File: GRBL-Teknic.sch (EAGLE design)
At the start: 9 parts

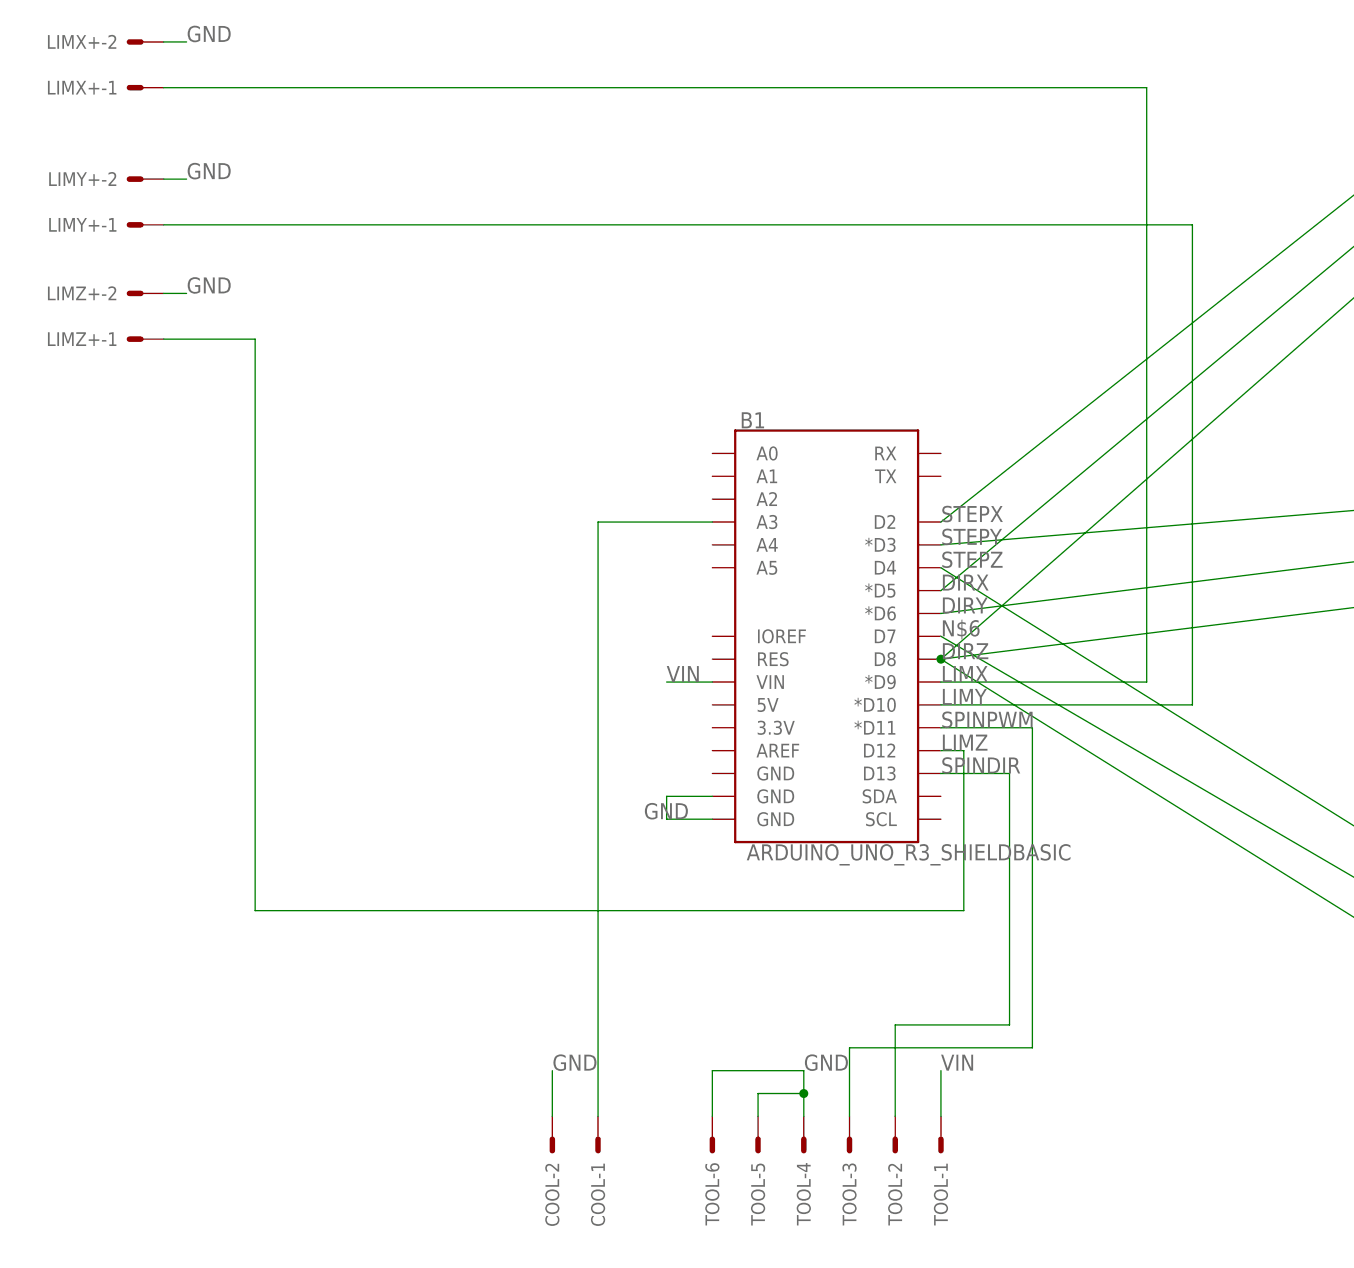
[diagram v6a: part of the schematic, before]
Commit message: updated as I learn more from EMI filtering
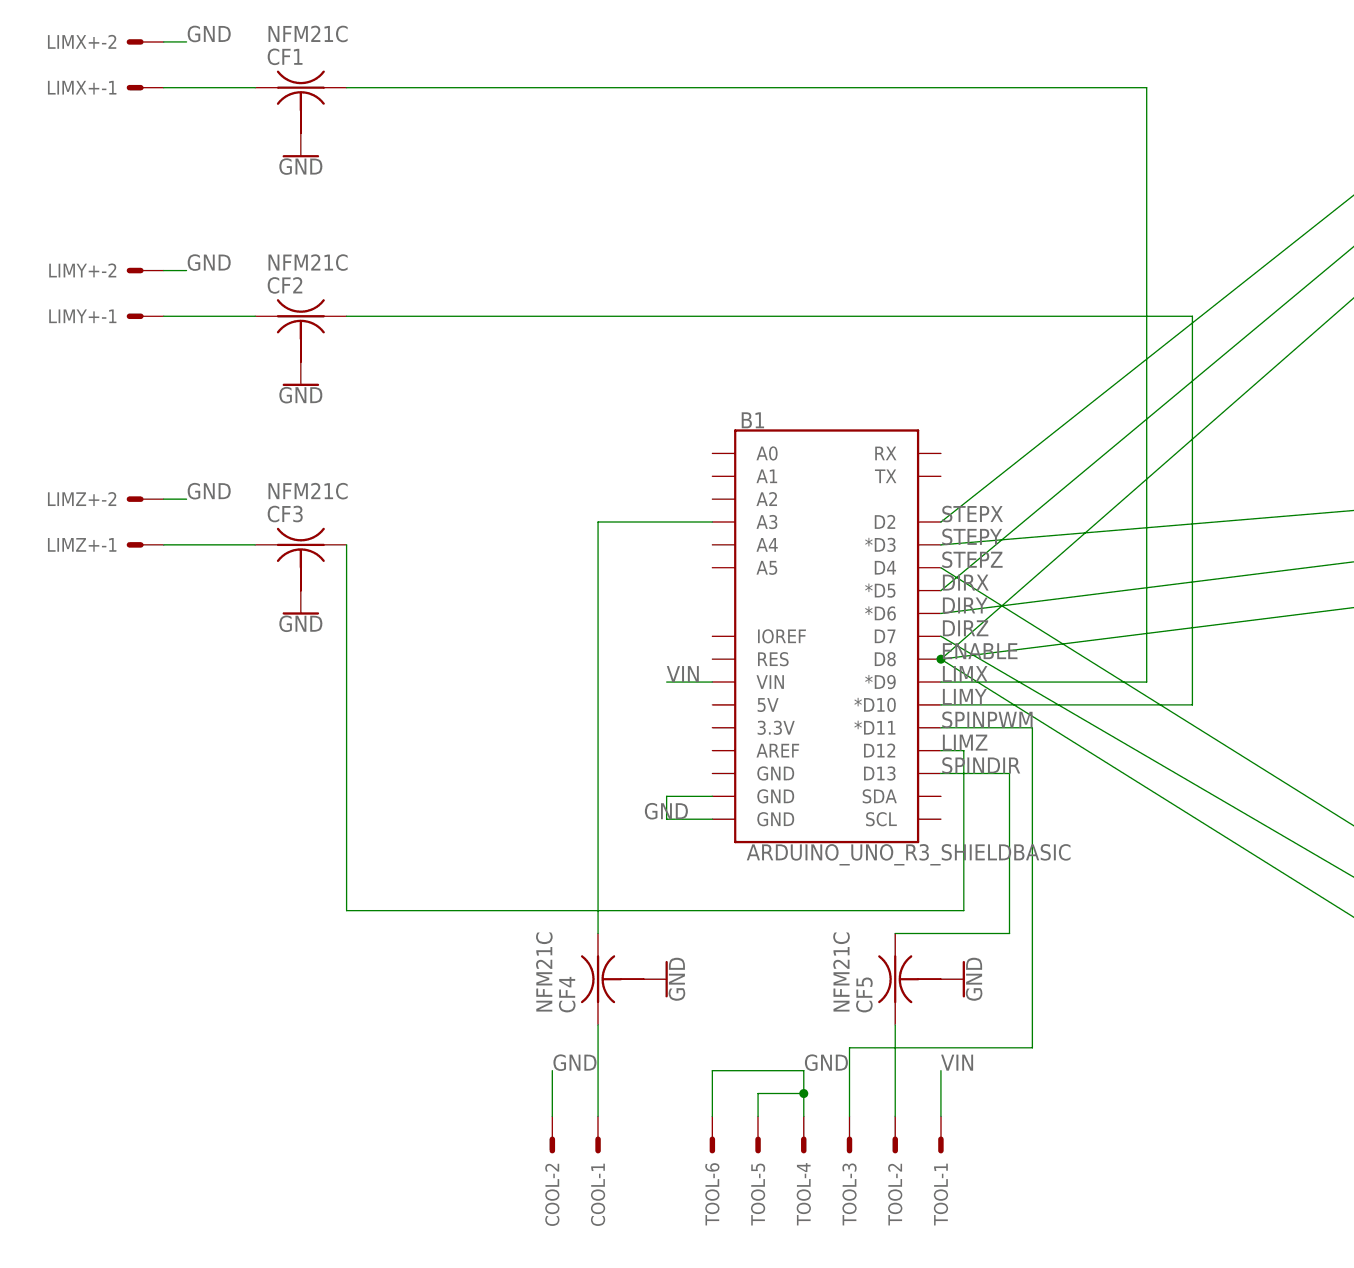
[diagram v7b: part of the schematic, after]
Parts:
- added CF1, CF2, CF3, CF4, CF5: NFM21C, murata-filter:NFM21C
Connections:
- removed net N$6: B1.D7, MOTORZ-3.S
- new net ENABLE: B1.D8, MOTORX-4.S, MOTORY-4.S, MOTORZ-4.S
- new net N$1: CF4.1, COOL-1.S
- new net N$2: CF5.1, TOOL-2.S
- new net N$3: CF1.1, LIMX+-1.S
- new net N$4: CF2.1, LIMY+-1.S
- new net N$5: CF3.1, LIMZ+-1.S
- net COOL: now also CF4.3; no longer COOL-1.S
- net DIRZ: now also B1.D7, MOTORZ-3.S; no longer B1.D8, MOTORX-4.S, MOTORY-4.S, MOTORZ-4.S
- net GND: now also CF1.2@1, CF2.2@1, CF3.2@1, CF4.2@1, CF5.2@1
- net LIMX: now also CF1.3; no longer LIMX+-1.S
- net LIMY: now also CF2.3; no longer LIMY+-1.S
- net LIMZ: now also CF3.3; no longer LIMZ+-1.S
- net SPINDIR: now also CF5.3; no longer TOOL-2.S
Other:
- moved on the sheet: LIMY+-1, LIMY+-2, LIMZ+-1, LIMZ+-2
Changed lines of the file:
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@@
 <setting verticaltext="up"/>
 </settings>
-<grid distance="0.1" unitdist="inch" unit="inch" style="lines" multiple="1" display="yes" altdistance="0.01" altunitdist="inch" altunit="inch"/>
+<grid distance="0.1" unitdist="inch" unit="inch" style="lines" multiple="1" display="no" altdistance="0.01" altunitdist="inch" altunit="inch"/>
 <layers>
 <layer number="1" name="Top" color="4" fill="1" visible="no" active="no"/>
@@
 <part name="TOOL" library="con-molex-2" deviceset="555X-6" device="V"/>
 <part name="COOL" library="con-molex-2" deviceset="555X-2" device="V"/>
+<part name="CF1" library="murata-filter" deviceset="NFM" device="21C"/>
+<part name="CF2" library="murata-filter" deviceset="NFM" device="21C"/>
+<part name="CF3" library="murata-filter" deviceset="NFM" device="21C"/>
+<part name="GND1" library="SparkFun-PowerSymbols" deviceset="GND" device=""/>
+<part name="GND2" library="SparkFun-PowerSymbols" deviceset="GND" device=""/>
+<part name="GND3" library="SparkFun-PowerSymbols" deviceset="GND" device=""/>
+<part name="CF4" library="murata-filter" deviceset="NFM" device="21C"/>
+<part name="GND4" library="SparkFun-PowerSymbols" deviceset="GND" device=""/>
+<part name="CF5" library="murata-filter" deviceset="NFM" device="21C"/>
+<part name="GND5" library="SparkFun-PowerSymbols" deviceset="GND" device=""/>
 </parts>
 <sheets>
@@
 <instance part="LIMX+" gate="-1" x="-45.72" y="106.68" rot="R180"/>
 <instance part="LIMX+" gate="-2" x="-45.72" y="111.76" rot="R180"/>
-<instance part="LIMY+" gate="-1" x="-45.72" y="91.44" rot="R180"/>
-<instance part="LIMY+" gate="-2" x="-45.72" y="96.52" rot="R180"/>
-<instance part="LIMZ+" gate="-1" x="-45.72" y="78.74" rot="R180"/>
-<instance part="LIMZ+" gate="-2" x="-45.72" y="83.82" rot="R180"/>
+<instance part="LIMY+" gate="-1" x="-45.72" y="81.28" rot="R180"/>
+<instance part="LIMY+" gate="-2" x="-45.72" y="86.36" rot="R180"/>
+<instance part="LIMZ+" gate="-1" x="-45.72" y="55.88" rot="R180"/>
+<instance part="LIMZ+" gate="-2" x="-45.72" y="60.96" rot="R180"/>
 <instance part="TOOL" gate="-1" x="43.18" y="-10.16" rot="R270"/>
 <instance part="TOOL" gate="-2" x="38.1" y="-10.16" rot="R270"/>
@@
 <instance part="COOL" gate="-1" x="5.08" y="-10.16" rot="R270"/>
 <instance part="COOL" gate="-2" x="0" y="-10.16" rot="R270"/>
+<instance part="CF1" gate="G$1" x="-27.94" y="106.68"/>
+<instance part="CF2" gate="G$1" x="-27.94" y="81.28"/>
+<instance part="CF3" gate="G$1" x="-27.94" y="55.88"/>
+<instance part="GND1" gate="1" x="-27.94" y="48.26"/>
+<instance part="GND2" gate="1" x="-27.94" y="99.06"/>
+<instance part="GND3" gate="1" x="-27.94" y="73.66"/>
+<instance part="CF4" gate="G$1" x="5.08" y="7.62" rot="R90"/>
+<instance part="GND4" gate="1" x="12.7" y="7.62" rot="R90"/>
+<instance part="CF5" gate="G$1" x="38.1" y="7.62" rot="R90"/>
+<instance part="GND5" gate="1" x="45.72" y="7.62" rot="R90"/>
 </instances>
 <busses>
@@
 </segment>
 <segment>
-<wire x1="-40.64" y1="83.82" x2="-43.18" y2="83.82" width="0.1524" layer="91"/>
-<label x="-40.64" y="83.82" size="1.778" layer="95"/>
+<wire x1="-40.64" y1="60.96" x2="-43.18" y2="60.96" width="0.1524" layer="91"/>
+<label x="-40.64" y="60.96" size="1.778" layer="95"/>
 <pinref part="LIMZ+" gate="-2" pin="S"/>
 </segment>
 <segment>
-<wire x1="-40.64" y1="96.52" x2="-43.18" y2="96.52" width="0.1524" layer="91"/>
-<label x="-40.64" y="96.52" size="1.778" layer="95"/>
+<wire x1="-40.64" y1="86.36" x2="-43.18" y2="86.36" width="0.1524" layer="91"/>
+<label x="-40.64" y="86.36" size="1.778" layer="95"/>
 <pinref part="LIMY+" gate="-2" pin="S"/>
 </segment>
@@
 <pinref part="COOL" gate="-2" pin="S"/>
 </segment>
+<segment>
+<pinref part="CF3" gate="G$1" pin="2@1"/>
+<pinref part="GND1" gate="1" pin="GND"/>
+</segment>
+<segment>
+<pinref part="CF1" gate="G$1" pin="2@1"/>
+<pinref part="GND2" gate="1" pin="GND"/>
+</segment>
+<segment>
+<pinref part="CF2" gate="G$1" pin="2@1"/>
+<pinref part="GND3" gate="1" pin="GND"/>
+</segment>
+<segment>
+<pinref part="CF4" gate="G$1" pin="2@1"/>
+<pinref part="GND4" gate="1" pin="GND"/>
+</segment>
+<segment>
+<pinref part="CF5" gate="G$1" pin="2@1"/>
+<pinref part="GND5" gate="1" pin="GND"/>
+</segment>
 </net>
 <net name="VIN" class="0">
@@
 <pinref part="B1" gate="G$1" pin="D13"/>
 <wire x1="43.18" y1="30.48" x2="50.8" y2="30.48" width="0.1524" layer="91"/>
-<wire x1="50.8" y1="30.48" x2="50.8" y2="2.54" width="0.1524" layer="91"/>
-<wire x1="50.8" y1="2.54" x2="38.1" y2="2.54" width="0.1524" layer="91"/>
-<pinref part="TOOL" gate="-2" pin="S"/>
-<wire x1="38.1" y1="2.54" x2="38.1" y2="-7.62" width="0.1524" layer="91"/>
 <label x="43.18" y="30.48" size="1.778" layer="95"/>
+<pinref part="CF5" gate="G$1" pin="3"/>
+<wire x1="38.1" y1="12.7" x2="50.8" y2="12.7" width="0.1524" layer="91"/>
+<wire x1="50.8" y1="12.7" x2="50.8" y2="30.48" width="0.1524" layer="91"/>
 </segment>
 </net>
@@
 <wire x1="43.18" y1="33.02" x2="45.72" y2="33.02" width="0.1524" layer="91"/>
 <wire x1="45.72" y1="33.02" x2="45.72" y2="15.24" width="0.1524" layer="91"/>
-<pinref part="LIMZ+" gate="-1" pin="S"/>
-<wire x1="-43.18" y1="78.74" x2="-33.02" y2="78.74" width="0.1524" layer="91"/>
-<wire x1="-33.02" y1="78.74" x2="-33.02" y2="15.24" width="0.1524" layer="91"/>
-<wire x1="-33.02" y1="15.24" x2="45.72" y2="15.24" width="0.1524" layer="91"/>
 <label x="43.18" y="33.02" size="1.778" layer="95"/>
+<wire x1="-22.86" y1="15.24" x2="45.72" y2="15.24" width="0.1524" layer="91"/>
+<pinref part="CF3" gate="G$1" pin="3"/>
+<wire x1="-22.86" y1="55.88" x2="-22.86" y2="15.24" width="0.1524" layer="91"/>
 </segment>
 </net>
@@
 <pinref part="B1" gate="G$1" pin="*D9"/>
 <wire x1="43.18" y1="40.64" x2="66.04" y2="40.64" width="0.1524" layer="91"/>
-<pinref part="LIMX+" gate="-1" pin="S"/>
 <wire x1="66.04" y1="40.64" x2="66.04" y2="106.68" width="0.1524" layer="91"/>
-<wire x1="66.04" y1="106.68" x2="-43.18" y2="106.68" width="0.1524" layer="91"/>
 <label x="43.18" y="40.64" size="1.778" layer="95"/>
+<pinref part="CF1" gate="G$1" pin="3"/>
+<wire x1="-22.86" y1="106.68" x2="66.04" y2="106.68" width="0.1524" layer="91"/>
 </segment>
 </net>
@@
 <pinref part="B1" gate="G$1" pin="*D10"/>
 <wire x1="43.18" y1="38.1" x2="71.12" y2="38.1" width="0.1524" layer="91"/>
-<pinref part="LIMY+" gate="-1" pin="S"/>
-<wire x1="-43.18" y1="91.44" x2="71.12" y2="91.44" width="0.1524" layer="91"/>
-<wire x1="71.12" y1="91.44" x2="71.12" y2="38.1" width="0.1524" layer="91"/>
+<wire x1="71.12" y1="81.28" x2="71.12" y2="38.1" width="0.1524" layer="91"/>
 <label x="43.18" y="38.1" size="1.778" layer="95"/>
+<pinref part="CF2" gate="G$1" pin="3"/>
+<wire x1="-22.86" y1="81.28" x2="71.12" y2="81.28" width="0.1524" layer="91"/>
 </segment>
 </net>
@@
 </segment>
 </net>
-<net name="N$6" class="0">
+<net name="DIRZ" class="0">
 <segment>
 <pinref part="MOTORZ" gate="-3" pin="S"/>
@@
 </segment>
 </net>
-<net name="DIRZ" class="0">
+<net name="ENABLE" class="0">
 <segment>
 <pinref part="MOTORX" gate="-4" pin="S"/>
@@
 <net name="COOL" class="0">
 <segment>
-<pinref part="COOL" gate="-1" pin="S"/>
-<wire x1="5.08" y1="-7.62" x2="5.08" y2="58.42" width="0.1524" layer="91"/>
 <pinref part="B1" gate="G$1" pin="A3"/>
 <wire x1="5.08" y1="58.42" x2="17.78" y2="58.42" width="0.1524" layer="91"/>
-</segment>
-</net>
+<pinref part="CF4" gate="G$1" pin="3"/>
+<wire x1="5.08" y1="12.7" x2="5.08" y2="58.42" width="0.1524" layer="91"/>
+</segment>
+</net>
+<net name="N$1" class="0">
+<segment>
+<pinref part="CF4" gate="G$1" pin="1"/>
+<pinref part="COOL" gate="-1" pin="S"/>
+<wire x1="5.08" y1="2.54" x2="5.08" y2="-7.62" width="0.1524" layer="91"/>
+</segment>
+</net>
+<net name="N$2" class="0">
+<segment>
+<pinref part="TOOL" gate="-2" pin="S"/>
+<wire x1="38.1" y1="2.54" x2="38.1" y2="-7.62" width="0.1524" layer="91"/>
+<pinref part="CF5" gate="G$1" pin="1"/>
+</segment>
+</net>
+<net name="N$3" class="0">
+<segment>
+<pinref part="CF1" gate="G$1" pin="1"/>
+<pinref part="LIMX+" gate="-1" pin="S"/>
+<wire x1="-33.02" y1="106.68" x2="-43.18" y2="106.68" width="0.1524" layer="91"/>
+</segment>
+</net>
+<net name="N$4" class="0">
+<segment>
+<pinref part="CF2" gate="G$1" pin="1"/>
+<pinref part="LIMY+" gate="-1" pin="S"/>
+<wire x1="-33.02" y1="81.28" x2="-43.18" y2="81.28" width="0.1524" layer="91"/>
+</segment>
+</net>
+<net name="N$5" class="0">
+<segment>
+<pinref part="CF3" gate="G$1" pin="1"/>
+<pinref part="LIMZ+" gate="-1" pin="S"/>
+<wire x1="-33.02" y1="55.88" x2="-43.18" y2="55.88" width="0.1524" layer="91"/>
+</segment>
+</net>
